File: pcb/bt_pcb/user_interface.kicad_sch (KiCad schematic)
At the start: 77 parts, among them J10 Conn_01x04, J11 Conn_01x04, J12 Conn_01x05, J7 Conn_01x04, J8 Conn_01x10, J9 Conn_01x04, SW1 SW_Push, SW2 SW_Push, SW3 SW_Push, SW4 SW_Push, SW5 SW_Push, SW6 SW_Push, SW7 SW_Push, SW8 SW_Push, SW9 SW_Push

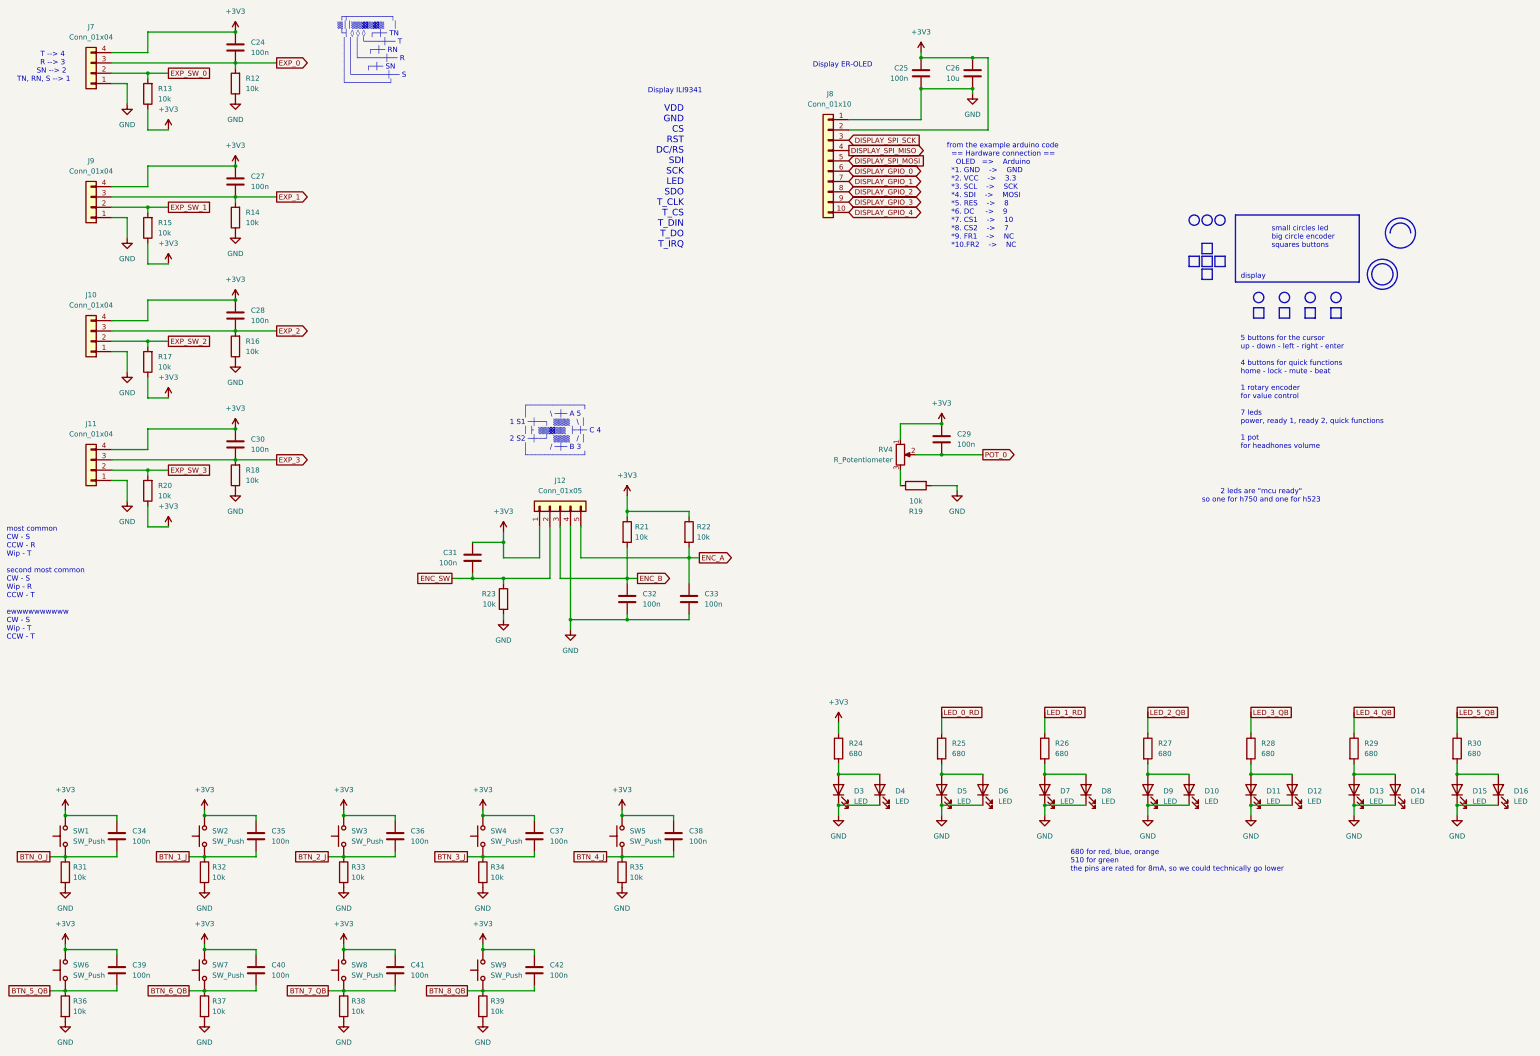
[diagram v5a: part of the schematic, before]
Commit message: pcb with some schematic tuning
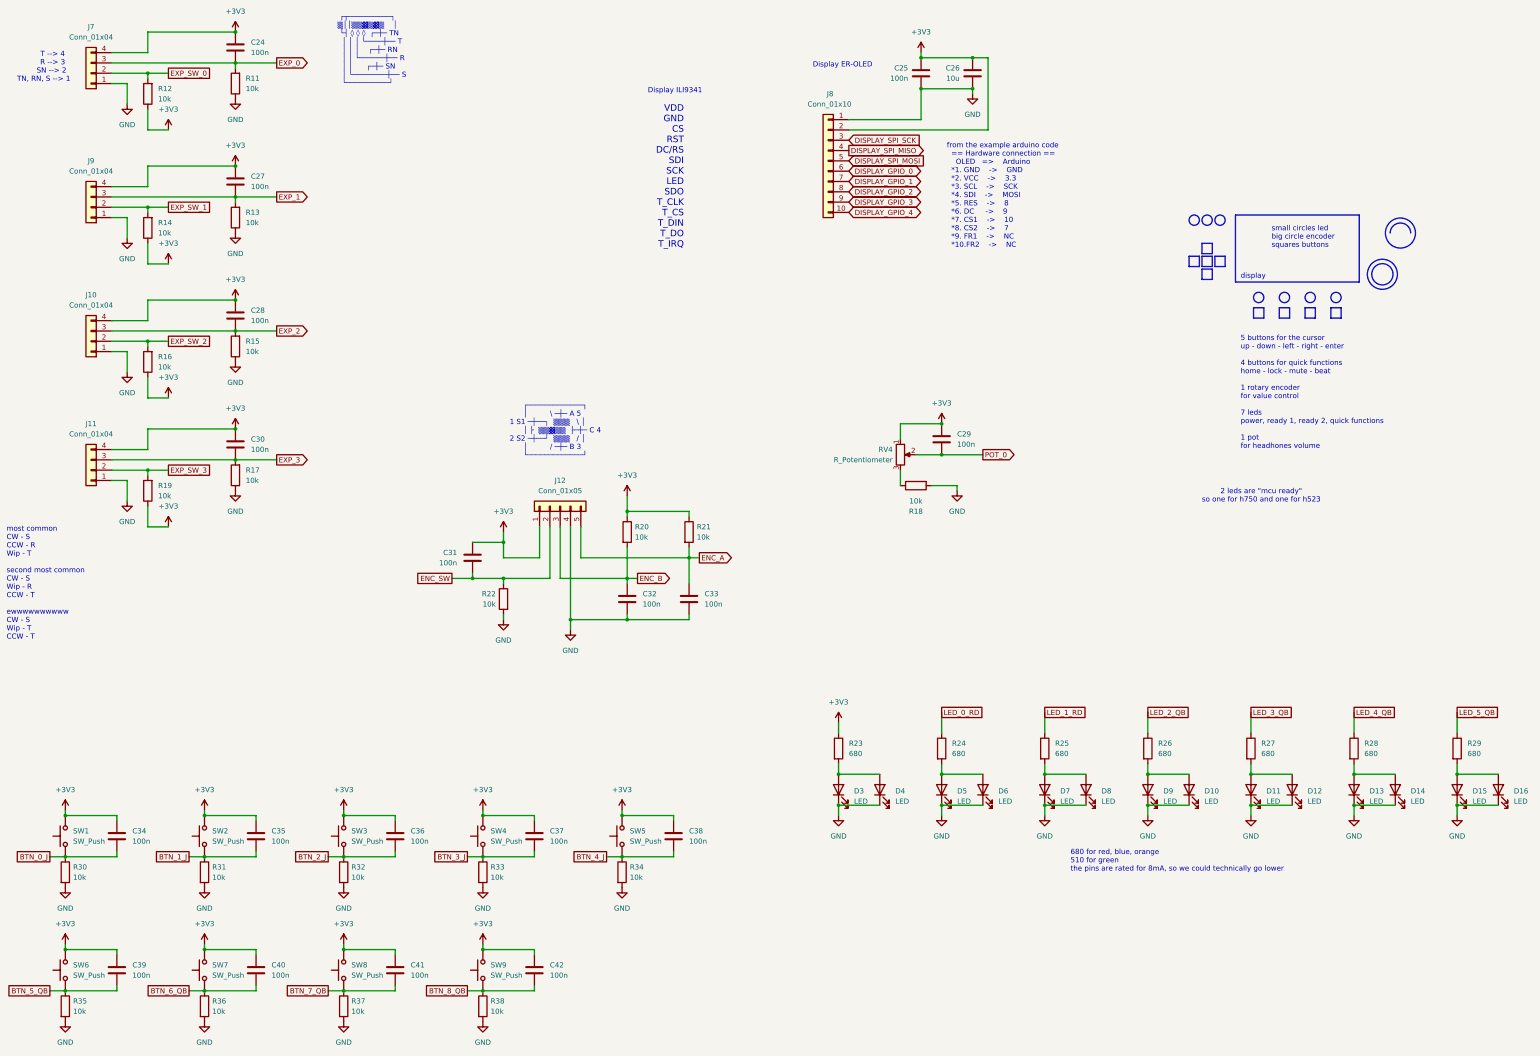
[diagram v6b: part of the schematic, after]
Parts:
- renumbered R12 to R11, R13 to R12, R14 to R13, R15 to R14, R16 to R15, R17 to R16, R18 to R17, R19 to R18, R20 to R19, R21 to R20, R22 to R21, R23 to R22, R24 to R23, R25 to R24, R26 to R25, R27 to R26, R28 to R27, R29 to R28, R30 to R29, R31 to R30, R32 to R31, R33 to R32, R34 to R33, R35 to R34, R36 to R35, R37 to R36, R38 to R37, R39 to R38

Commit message: pcb now under revision
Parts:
- added C46: 100n, Capacitor_SMD:C_0603_1608Metric_Pad1.08x0.95mm_HandSolder, symbol Device:C
- added R39: 10k, Resistor_SMD:R_0603_1608Metric_Pad0.98x0.95mm_HandSolder, symbol Device:R
- added SW10: SW_Push, Button_Switch_THT:SW_TH_Tactile_Omron_B3F-102x, symbol Switch:SW_Push
- renumbered C24 to C27, C25 to C28, C26 to C29, C27 to C30, C28 to C31, C29 to C32, C30 to C33, C31 to C34, C32 to C35, C33 to C36, C34 to C37, C35 to C38, C36 to C39, C37 to C40, C38 to C41, C39 to C42, C40 to C43, C41 to C44, C42 to C45
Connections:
- net +3V3: now also C46.1, SW10.2
- net GND: now also R39.2
- new net BTN_9_J: C46.2, R39.1, SW10.1

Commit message: first notes
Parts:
- removed C37, C38, C39, C40, C41, C42, C43, C44, C45, C46: 100n, Capacitor_SMD:C_0603_1608Metric_Pad1.08x0.95mm_HandSolder, symbol Device:C
- removed R18: 10k, Resistor_SMD:R_0603_1608Metric_Pad0.98x0.95mm_HandSolder, symbol Device:R
- renumbered R19 to R18, R20 to R19, R21 to R20, R22 to R21, R23 to R22, R24 to R23, R25 to R24, R26 to R25, R27 to R26, R28 to R27, R29 to R28, R30 to R29, R31 to R30, R32 to R31, R33 to R32, R34 to R33, R35 to R34, R36 to R35, R37 to R36, R38 to R37, R39 to R38
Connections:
- net GND: now also RV4.3
